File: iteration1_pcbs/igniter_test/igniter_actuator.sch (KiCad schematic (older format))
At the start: 39 parts, among them IC1 LM51571QRTERQ1, J2 FET_A_P, J3 FET_A_N, J4 FET_B_P, J5 FET_B_N, Q1 STL36DN6F7, Q2 BSS138PW_115, U2 MIC4127YME-TR

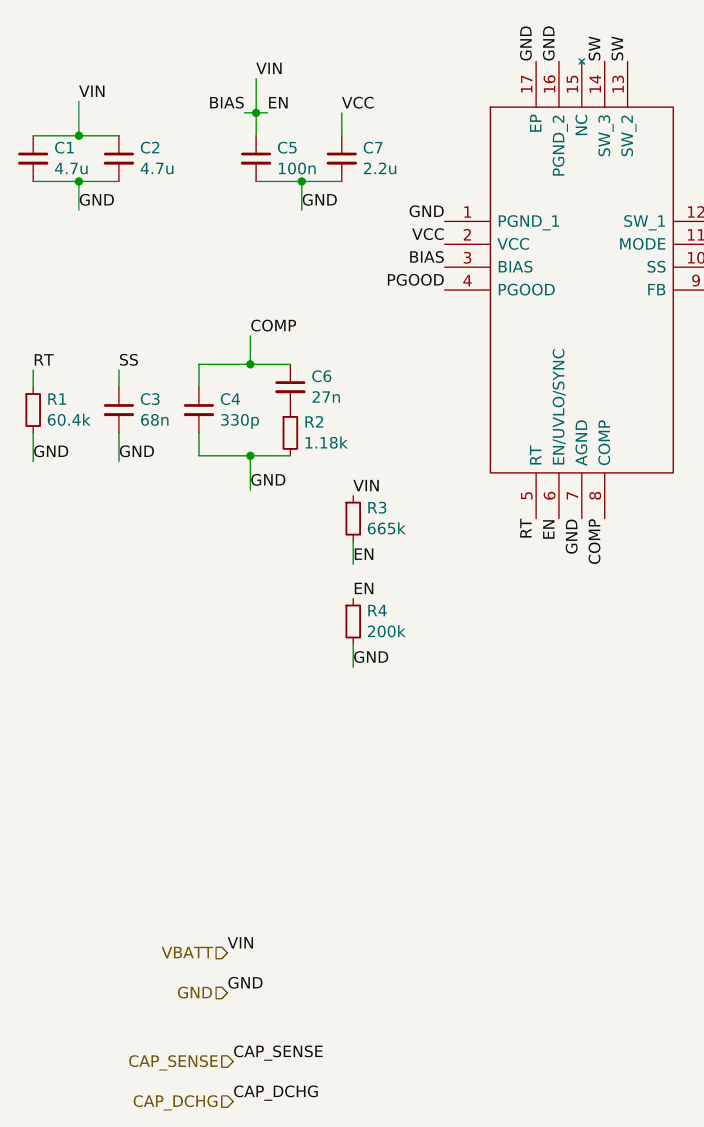
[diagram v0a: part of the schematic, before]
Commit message: Adding igniter testing
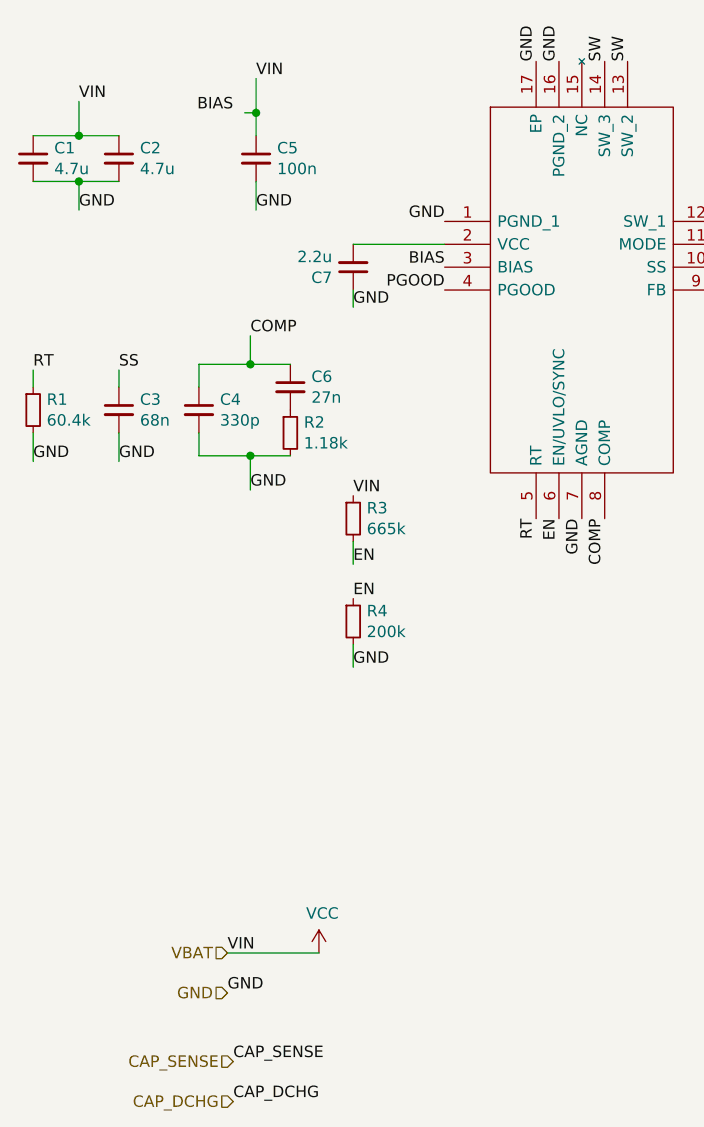
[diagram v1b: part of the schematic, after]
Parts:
- C1, C11, C2, C5, C6, C7: footprint (none) -> Capacitor_SMD:C_0805_2012Metric_Pad1.18x1.45mm_HandSolder
- C10, C8, C9: footprint (none) -> Capacitor_SMD:C_1206_3216Metric_Pad1.33x1.80mm_HandSolder
- C12: footprint (none) -> iteration1:UVR1H682MRD6
- C13, C14, C15, C3, C4: footprint (none) -> Capacitor_SMD:C_0603_1608Metric_Pad1.08x0.95mm_HandSolder
- J2, J3, J4, J5: footprint (none) -> iteration1:SM99S01VBNN05G7
- L1: footprint (none) -> Inductor_SMD:L_Wuerth_HCI-1365
- R1, R10, R11, R12, R2, R5, R6, R7, R8, R9: footprint (none) -> Resistor_SMD:R_0603_1608Metric_Pad0.98x0.95mm_HandSolder
- R14: footprint (none) -> Resistor_SMD:R_0805_2012Metric_Pad1.20x1.40mm_HandSolder
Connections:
- net GND: now also C7.1; no longer C7.2
- net VCC: now also C1.1, C13.1, C14.1, C15.1, C2.1, C5.1, L1.1, R3.1, U2.6 (VS); no longer C7.1, IC1.2 (VCC)
- removed net VBATT: C1.1, C13.1, C14.1, C15.1, C2.1, C5.1, IC1.3 (BIAS), IC1.6 (EN/UVLO/SYNC), L1.1, R3.1, R3.2, R4.1, U2.6 (VS)
- new net: C7.2, IC1.2 (VCC)
- new net BIAS: IC1.3 (BIAS)
- new net EN: IC1.6 (EN/UVLO/SYNC), R3.2, R4.1
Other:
- moved on the sheet: C7
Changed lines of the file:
@@
 F 0 "L1" V 4640 1375 50  0000 C CNN
 F 1 "15.4u" V 4549 1375 50  0000 C CNN
-F 2 "" H 4450 1375 50  0001 C CNN
+F 2 "Inductor_SMD:L_Wuerth_HCI-1365" H 4450 1375 50  0001 C CNN
 F 3 "~" H 4450 1375 50  0001 C CNN
 	1    4450 1375
@@
 Text Label 4600 1375 0    50   ~ 0
 SW
-$Comp
-L Device:C_Small C7
-U 1 1 60C69D5B
-P 2100 1275
-F 0 "C7" H 2192 1321 50  0000 L CNN
-F 1 "2.2u" H 2192 1230 50  0000 L CNN
-F 2 "" H 2100 1275 50  0001 C CNN
-F 3 "~" H 2100 1275 50  0001 C CNN
-	1    2100 1275
-	1    0    0    -1
-$EndComp
 $Comp
 L Device:C_Small C5
@@
 F 0 "C5" H 1817 1321 50  0000 L CNN
 F 1 "100n" H 1817 1230 50  0000 L CNN
-F 2 "" H 1725 1275 50  0001 C CNN
+F 2 "Capacitor_SMD:C_0805_2012Metric_Pad1.18x1.45mm_HandSolder" H 1725 1275 50  0001 C CNN
 F 3 "~" H 1725 1275 50  0001 C CNN
 	1    1725 1275
@@
 F 0 "C1" H 842 1321 50  0000 L CNN
 F 1 "4.7u" H 842 1230 50  0000 L CNN
-F 2 "" H 750 1275 50  0001 C CNN
+F 2 "Capacitor_SMD:C_0805_2012Metric_Pad1.18x1.45mm_HandSolder" H 750 1275 50  0001 C CNN
 F 3 "~" H 750 1275 50  0001 C CNN
 	1    750  1275
@@
 F 0 "C2" H 1217 1321 50  0000 L CNN
 F 1 "4.7u" H 1217 1230 50  0000 L CNN
-F 2 "" H 1125 1275 50  0001 C CNN
+F 2 "Capacitor_SMD:C_0805_2012Metric_Pad1.18x1.45mm_HandSolder" H 1125 1275 50  0001 C CNN
 F 3 "~" H 1125 1275 50  0001 C CNN
 	1    1125 1275
@@
 F 0 "C3" H 1217 2421 50  0000 L CNN
 F 1 "68n" H 1217 2330 50  0000 L CNN
-F 2 "" H 1125 2375 50  0001 C CNN
+F 2 "Capacitor_SMD:C_0603_1608Metric_Pad1.08x0.95mm_HandSolder" H 1125 2375 50  0001 C CNN
 F 3 "~" H 1125 2375 50  0001 C CNN
 	1    1125 2375
@@
 F 0 "C4" H 1567 2421 50  0000 L CNN
 F 1 "330p" H 1567 2330 50  0000 L CNN
-F 2 "" H 1475 2375 50  0001 C CNN
+F 2 "Capacitor_SMD:C_0603_1608Metric_Pad1.08x0.95mm_HandSolder" H 1475 2375 50  0001 C CNN
 F 3 "~" H 1475 2375 50  0001 C CNN
 	1    1475 2375
@@
 F 0 "C6" H 1967 2321 50  0000 L CNN
 F 1 "27n" H 1967 2230 50  0000 L CNN
-F 2 "" H 1875 2275 50  0001 C CNN
+F 2 "Capacitor_SMD:C_0805_2012Metric_Pad1.18x1.45mm_HandSolder" H 1875 2275 50  0001 C CNN
 F 3 "~" H 1875 2275 50  0001 C CNN
 	1    1875 2275
@@
 F 0 "R1" H 809 2421 50  0000 L CNN
 F 1 "60.4k" H 809 2330 50  0000 L CNN
-F 2 "" H 750 2375 50  0001 C CNN
+F 2 "Resistor_SMD:R_0603_1608Metric_Pad0.98x0.95mm_HandSolder" H 750 2375 50  0001 C CNN
 F 3 "~" H 750 2375 50  0001 C CNN
 	1    750  2375
@@
 F 0 "R2" H 1934 2521 50  0000 L CNN
 F 1 "1.18k" H 1934 2430 50  0000 L CNN
-F 2 "" H 1875 2475 50  0001 C CNN
+F 2 "Resistor_SMD:R_0603_1608Metric_Pad0.98x0.95mm_HandSolder" H 1875 2475 50  0001 C CNN
 F 3 "~" H 1875 2475 50  0001 C CNN
 	1    1875 2475
@@
 F 0 "R5" H 4534 2546 50  0000 L CNN
 F 1 "118k" H 4534 2455 50  0000 L CNN
-F 2 "" H 4475 2500 50  0001 C CNN
+F 2 "Resistor_SMD:R_0603_1608Metric_Pad0.98x0.95mm_HandSolder" H 4475 2500 50  0001 C CNN
 F 3 "~" H 4475 2500 50  0001 C CNN
 	1    4475 2500
@@
 F 0 "R6" H 4534 2846 50  0000 L CNN
 F 1 "2.49k" H 4534 2755 50  0000 L CNN
-F 2 "" H 4475 2800 50  0001 C CNN
+F 2 "Resistor_SMD:R_0603_1608Metric_Pad0.98x0.95mm_HandSolder" H 4475 2800 50  0001 C CNN
 F 3 "~" H 4475 2800 50  0001 C CNN
 	1    4475 2800
@@
 F 0 "C8" H 5217 1371 50  0000 L CNN
 F 1 "3.3u" H 5217 1280 50  0000 L CNN
-F 2 "" H 5125 1325 50  0001 C CNN
+F 2 "Capacitor_SMD:C_1206_3216Metric_Pad1.33x1.80mm_HandSolder" H 5125 1325 50  0001 C CNN
 F 3 "~" H 5125 1325 50  0001 C CNN
 	1    5125 1325
@@
 F 0 "C9" H 5592 1371 50  0000 L CNN
 F 1 "3.3u" H 5592 1280 50  0000 L CNN
-F 2 "" H 5500 1325 50  0001 C CNN
+F 2 "Capacitor_SMD:C_1206_3216Metric_Pad1.33x1.80mm_HandSolder" H 5500 1325 50  0001 C CNN
 F 3 "~" H 5500 1325 50  0001 C CNN
 	1    5500 1325
@@
 F 0 "C10" H 5942 1371 50  0000 L CNN
 F 1 "3.3u" H 5942 1280 50  0000 L CNN
-F 2 "" H 5850 1325 50  0001 C CNN
+F 2 "Capacitor_SMD:C_1206_3216Metric_Pad1.33x1.80mm_HandSolder" H 5850 1325 50  0001 C CNN
 F 3 "~" H 5850 1325 50  0001 C CNN
 	1    5850 1325
@@
 F 0 "C11" H 6392 1371 50  0000 L CNN
 F 1 "100n" H 6392 1280 50  0000 L CNN
-F 2 "" H 6300 1325 50  0001 C CNN
+F 2 "Capacitor_SMD:C_0805_2012Metric_Pad1.18x1.45mm_HandSolder" H 6300 1325 50  0001 C CNN
 F 3 "~" H 6300 1325 50  0001 C CNN
 	1    6300 1325
@@
 Wire Wire Line
 	950  1375 1125 1375
-Text Label 2550 1650 2    50   ~ 0
-VCC
-Text Label 2100 1075 0    50   ~ 0
-VCC
-Wire Wire Line
-	2100 1075 2100 1175
-Text Label 1925 1500 0    50   ~ 0
-GND
-Wire Wire Line
-	1925 1500 1925 1375
-Wire Wire Line
-	1725 1375 1925 1375
-Connection ~ 1925 1375
-Wire Wire Line
-	1925 1375 2100 1375
-Text Label 2550 1750 2    50   ~ 0
-BIAS
+Text Label 1725 1500 0    50   ~ 0
+GND
+Wire Wire Line
+	1725 1500 1725 1375
 Text Label 3050 2850 3    50   ~ 0
 EN
-Text Label 1675 1075 2    50   ~ 0
+Text Label 1625 1075 2    50   ~ 0
 BIAS
-Text Label 1775 1075 0    50   ~ 0
-EN
-Wire Wire Line
-	1775 1075 1725 1075
 Wire Wire Line
 	1725 1075 1725 1175
@@
 PGOOD
 Text HLabel 1600 4750 0    50   Input ~ 0
-VBATT
+VBAT
 Text HLabel 1600 4925 0    50   Input ~ 0
 GND
@@
 F 0 "C12" H 8165 2346 50  0000 L CNN
 F 1 "6800u" H 8165 2255 50  0000 L CNN
-F 2 "" H 8088 2150 50  0001 C CNN
+F 2 "iteration1:UVR1H682MRD6" H 8088 2150 50  0001 C CNN
 F 3 "~" H 8050 2300 50  0001 C CNN
 	1    8050 2300
@@
 F 0 "R14" H 9445 2071 50  0000 L CNN
 F 1 "10k" H 9445 1980 50  0000 L CNN
-F 2 "" V 9305 2025 50  0001 C CNN
+F 2 "Resistor_SMD:R_0805_2012Metric_Pad1.20x1.40mm_HandSolder" V 9305 2025 50  0001 C CNN
 F 3 "~" H 9375 2025 50  0001 C CNN
 	1    9375 2025
@@
 F 0 "C14" H 9467 3971 50  0000 L CNN
 F 1 "0.1u" H 9467 3880 50  0000 L CNN
-F 2 "" H 9375 3925 50  0001 C CNN
+F 2 "Capacitor_SMD:C_0603_1608Metric_Pad1.08x0.95mm_HandSolder" H 9375 3925 50  0001 C CNN
 F 3 "~" H 9375 3925 50  0001 C CNN
 	1    9375 3925
@@
 F 0 "C15" H 9817 3971 50  0000 L CNN
 F 1 "1u" H 9817 3880 50  0000 L CNN
-F 2 "" H 9725 3925 50  0001 C CNN
+F 2 "Capacitor_SMD:C_0603_1608Metric_Pad1.08x0.95mm_HandSolder" H 9725 3925 50  0001 C CNN
 F 3 "~" H 9725 3925 50  0001 C CNN
 	1    9725 3925
@@
 F 0 "C13" H 9117 3971 50  0000 L CNN
 F 1 "0.1u" H 9117 3880 50  0000 L CNN
-F 2 "" H 9025 3925 50  0001 C CNN
+F 2 "Capacitor_SMD:C_0603_1608Metric_Pad1.08x0.95mm_HandSolder" H 9025 3925 50  0001 C CNN
 F 3 "~" H 9025 3925 50  0001 C CNN
 	1    9025 3925
@@
 F 0 "J2" H 9805 4667 50  0000 L CNN
 F 1 "FET_A_P" H 9805 4576 50  0000 L CNN
-F 2 "" H 9725 4625 50  0001 C CNN
+F 2 "iteration1:SM99S01VBNN05G7" H 9725 4625 50  0001 C CNN
 F 3 "~" H 9725 4625 50  0001 C CNN
 	1    9725 4625
@@
 F 0 "J3" H 9805 4942 50  0000 L CNN
 F 1 "FET_A_N" H 9805 4851 50  0000 L CNN
-F 2 "" H 9725 4900 50  0001 C CNN
+F 2 "iteration1:SM99S01VBNN05G7" H 9725 4900 50  0001 C CNN
 F 3 "~" H 9725 4900 50  0001 C CNN
 	1    9725 4900
@@
 F 0 "J4" H 9805 5217 50  0000 L CNN
 F 1 "FET_B_P" H 9805 5126 50  0000 L CNN
-F 2 "" H 9725 5175 50  0001 C CNN
+F 2 "iteration1:SM99S01VBNN05G7" H 9725 5175 50  0001 C CNN
 F 3 "~" H 9725 5175 50  0001 C CNN
 	1    9725 5175
@@
 F 0 "J5" H 9805 5492 50  0000 L CNN
 F 1 "FET_B_N" H 9805 5401 50  0000 L CNN
-F 2 "" H 9725 5450 50  0001 C CNN
+F 2 "iteration1:SM99S01VBNN05G7" H 9725 5450 50  0001 C CNN
 F 3 "~" H 9725 5450 50  0001 C CNN
 	1    9725 5450
@@
 F 0 "R11" H 6709 5196 50  0000 L CNN
 F 1 "120k" H 6709 5105 50  0000 L CNN
-F 2 "" H 6650 5150 50  0001 C CNN
+F 2 "Resistor_SMD:R_0603_1608Metric_Pad0.98x0.95mm_HandSolder" H 6650 5150 50  0001 C CNN
 F 3 "~" H 6650 5150 50  0001 C CNN
 	1    6650 5150
@@
 F 0 "R12" H 6709 5571 50  0000 L CNN
 F 1 "8.2k" H 6709 5480 50  0000 L CNN
-F 2 "" H 6650 5525 50  0001 C CNN
+F 2 "Resistor_SMD:R_0603_1608Metric_Pad0.98x0.95mm_HandSolder" H 6650 5525 50  0001 C CNN
 F 3 "~" H 6650 5525 50  0001 C CNN
 	1    6650 5525
@@
 F 0 "R10" H 6059 5571 50  0000 L CNN
 F 1 "8.2k" H 6059 5480 50  0000 L CNN
-F 2 "" H 6000 5525 50  0001 C CNN
+F 2 "Resistor_SMD:R_0603_1608Metric_Pad0.98x0.95mm_HandSolder" H 6000 5525 50  0001 C CNN
 F 3 "~" H 6000 5525 50  0001 C CNN
 	1    6000 5525
@@
 F 0 "R9" H 6059 5196 50  0000 L CNN
 F 1 "120k" H 6059 5105 50  0000 L CNN
-F 2 "" H 6000 5150 50  0001 C CNN
+F 2 "Resistor_SMD:R_0603_1608Metric_Pad0.98x0.95mm_HandSolder" H 6000 5150 50  0001 C CNN
 F 3 "~" H 6000 5150 50  0001 C CNN
 	1    6000 5150
@@
 F 0 "R8" H 5309 5571 50  0000 L CNN
 F 1 "8.2k" H 5309 5480 50  0000 L CNN
-F 2 "" H 5250 5525 50  0001 C CNN
+F 2 "Resistor_SMD:R_0603_1608Metric_Pad0.98x0.95mm_HandSolder" H 5250 5525 50  0001 C CNN
 F 3 "~" H 5250 5525 50  0001 C CNN
 	1    5250 5525
@@
 F 0 "R7" H 5309 5196 50  0000 L CNN
 F 1 "120k" H 5309 5105 50  0000 L CNN
-F 2 "" H 5250 5150 50  0001 C CNN
+F 2 "Resistor_SMD:R_0603_1608Metric_Pad0.98x0.95mm_HandSolder" H 5250 5150 50  0001 C CNN
 F 3 "~" H 5250 5150 50  0001 C CNN
 	1    5250 5150
 	1    0    0    -1
 $EndComp
+Text Label 2550 1750 2    50   ~ 0
+BIAS
+$Comp
+L Device:C_Small C7
+U 1 1 60C69D5B
+P 2150 1750
+F 0 "C7" H 2242 1796 50  0000 L CNN
+F 1 "2.2u" H 2242 1705 50  0000 L CNN
+F 2 "Capacitor_SMD:C_0805_2012Metric_Pad1.18x1.45mm_HandSolder" H 2150 1750 50  0001 C CNN
+F 3 "~" H 2150 1750 50  0001 C CNN
+	1    2150 1750
+	-1   0    0    1
+$EndComp
+Wire Wire Line
+	2150 1650 2550 1650
+Wire Wire Line
+	2150 1850 2150 1925
+Text Label 2150 1925 0    50   ~ 0
+GND
+Wire Wire Line
+	1600 4750 2000 4750
+$Comp
+L power:VCC #PWR?
+U 1 1 60F1EC83
+P 2000 4750
+F 0 "#PWR?" H 2000 4600 50  0001 C CNN
+F 1 "VCC" H 2015 4923 50  0000 C CNN
+F 2 "" H 2000 4750 50  0001 C CNN
+F 3 "" H 2000 4750 50  0001 C CNN
+	1    2000 4750
+	1    0    0    -1
+$EndComp

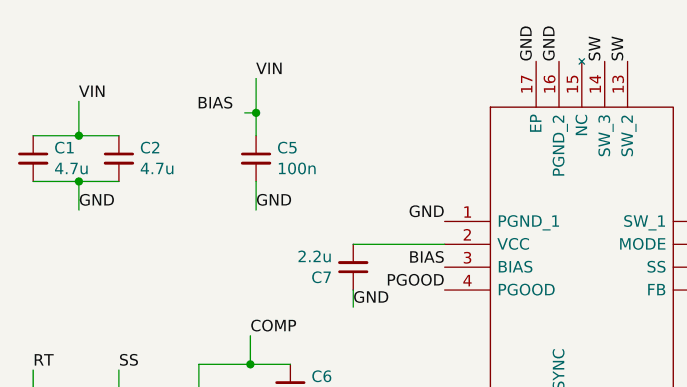
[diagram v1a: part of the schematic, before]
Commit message: Laying out and wiring the igniter test pcb
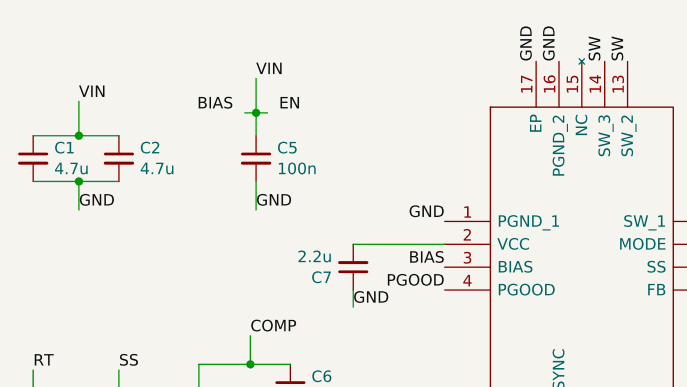
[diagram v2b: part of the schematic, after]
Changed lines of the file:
@@
 	1    0    0    -1
 $EndComp
+Text Label 1825 1075 0    50   ~ 0
+EN
+Wire Wire Line
+	1775 1075 1725 1075
 $EndSCHEMATC

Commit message: igniter test tracks
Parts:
- added R15: 37.4k, Resistor_SMD:R_0603_1608Metric_Pad0.98x0.95mm_HandSolder, symbol Device:R_Small
- R3: value 665k -> 274k; footprint Resistor_SMD:R_0805_2012Metric_Pad1.20x1.40mm_HandSolder -> Resistor_SMD:R_0603_1608Metric_Pad0.98x0.95mm_HandSolder
- R4: value 200k -> 95.3k
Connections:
- net GND: now also R15.2; no longer IC1.11 (MODE)
- new net MODE: IC1.11 (MODE), R15.1
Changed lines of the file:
@@
 Wire Wire Line
 	750  2475 750  2600
-Text Label 3750 1650 0    50   ~ 0
+Text Label 3800 2600 0    50   ~ 0
 GND
 Text Label 3750 1750 0    50   ~ 0
@@
 AR Path="/60E9633F/60D8653B" Ref="R3"  Part="1"
 F 0 "R3" H 2209 2896 50  0000 L CNN
-F 1 "665k" H 2209 2805 50  0000 L CNN
-F 2 "Resistor_SMD:R_0805_2012Metric_Pad1.20x1.40mm_HandSolder" H 2150 2850 50  0001 C CNN
+F 1 "274k" H 2209 2805 50  0000 L CNN
+F 2 "Resistor_SMD:R_0603_1608Metric_Pad0.98x0.95mm_HandSolder" H 2150 2850 50  0001 C CNN
 F 3 "~" H 2150 2850 50  0001 C CNN
 	1    2150 2850
@@
 AR Path="/60E9633F/60D86544" Ref="R4"  Part="1"
 F 0 "R4" H 2209 3346 50  0000 L CNN
-F 1 "200k" H 2209 3255 50  0000 L CNN
+F 1 "95.3k" H 2209 3255 50  0000 L CNN
 F 2 "Resistor_SMD:R_0603_1608Metric_Pad0.98x0.95mm_HandSolder" H 2150 3300 50  0001 C CNN
 F 3 "~" H 2150 3300 50  0001 C CNN
@@
 	1600 4750 2000 4750
 $Comp
-L power:VCC #PWR?
+L power:VCC #PWR0101
 U 1 1 60F1EC83
 P 2000 4750
-F 0 "#PWR?" H 2000 4600 50  0001 C CNN
+F 0 "#PWR0101" H 2000 4600 50  0001 C CNN
 F 1 "VCC" H 2015 4923 50  0000 C CNN
 F 2 "" H 2000 4750 50  0001 C CNN
@@
 	1    0    0    -1
 $EndComp
-Text Label 1825 1075 0    50   ~ 0
-EN
-Wire Wire Line
-	1775 1075 1725 1075
+Text Label 3750 1650 0    50   ~ 0
+MODE
+Text Label 3800 2325 0    50   ~ 0
+MODE
+$Comp
+L Device:R_Small R15
+U 1 1 60FBB719
+P 3800 2425
+F 0 "R15" H 3859 2471 50  0000 L CNN
+F 1 "37.4k" H 3859 2380 50  0000 L CNN
+F 2 "Resistor_SMD:R_0603_1608Metric_Pad0.98x0.95mm_HandSolder" H 3800 2425 50  0001 C CNN
+F 3 "~" H 3800 2425 50  0001 C CNN
+	1    3800 2425
+	1    0    0    -1
+$EndComp
+Wire Wire Line
+	3800 2525 3800 2600
 $EndSCHEMATC
